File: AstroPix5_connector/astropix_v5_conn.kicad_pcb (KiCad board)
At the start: 4 copper layers, 56.4 x 65.6 mm, 51 parts, among them J1 HBOut, J10 SPI_right, J12 Measures_Analog, J14 Bias, J2 Conn_01x05, J3 pcie_GECCO, J4 HBOut, J5 HBOut, J7 HV_in_external, J8 Conn_01x03, J9 SPI_left, U2 AstroPix5_split_powerring

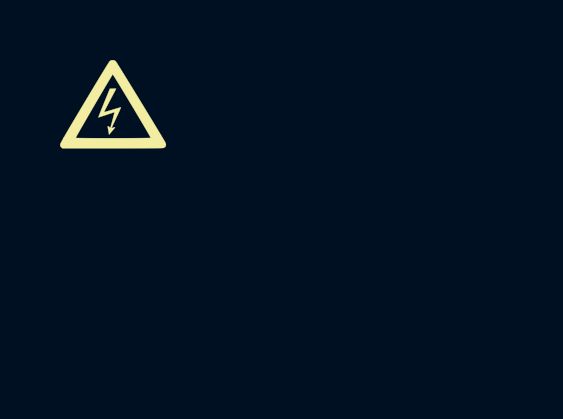
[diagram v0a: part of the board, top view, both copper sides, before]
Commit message: Fix BOM: separate C14/C15 (500V/1210) from standard capacitors
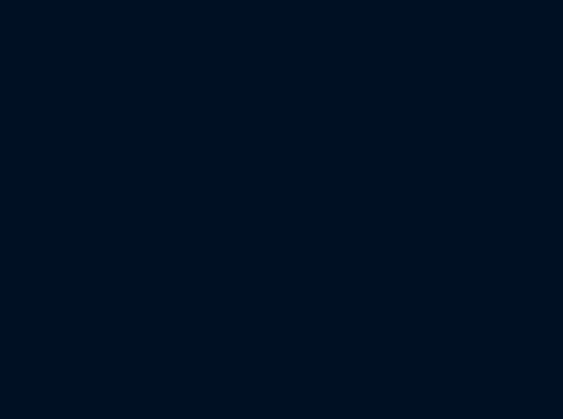
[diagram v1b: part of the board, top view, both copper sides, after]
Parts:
- removed Logo6: HV_logo, astropix:hv
